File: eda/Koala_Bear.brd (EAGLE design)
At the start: 31.9 x 40 mm, 23 parts

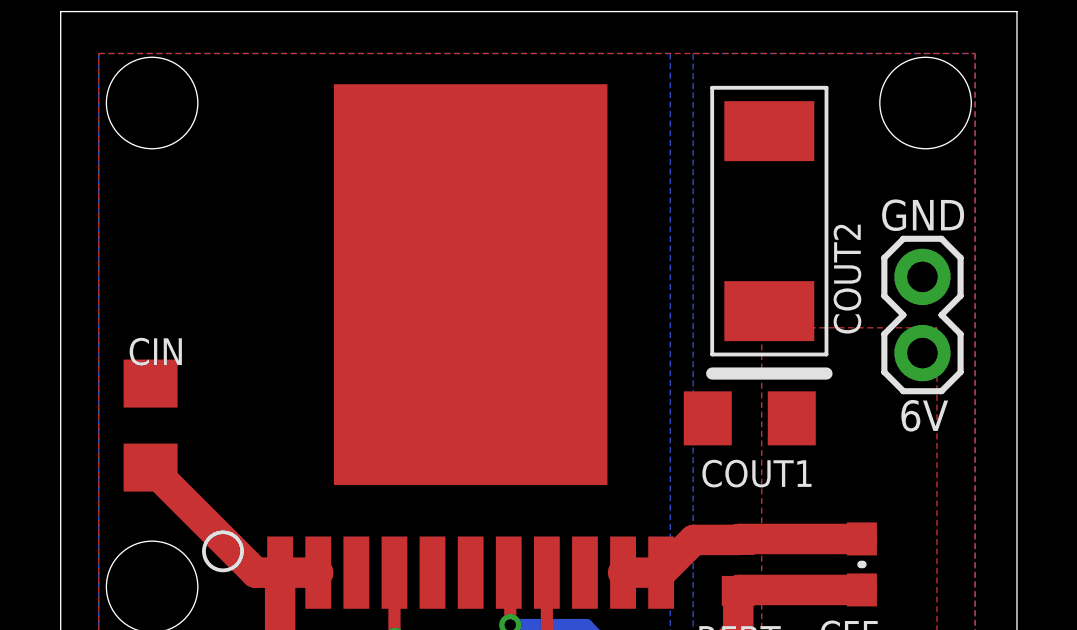
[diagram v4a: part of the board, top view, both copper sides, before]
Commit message: Ribboncable pinout fixed.
On battery_buzzer, smartsensor, and smartsensorPowered.
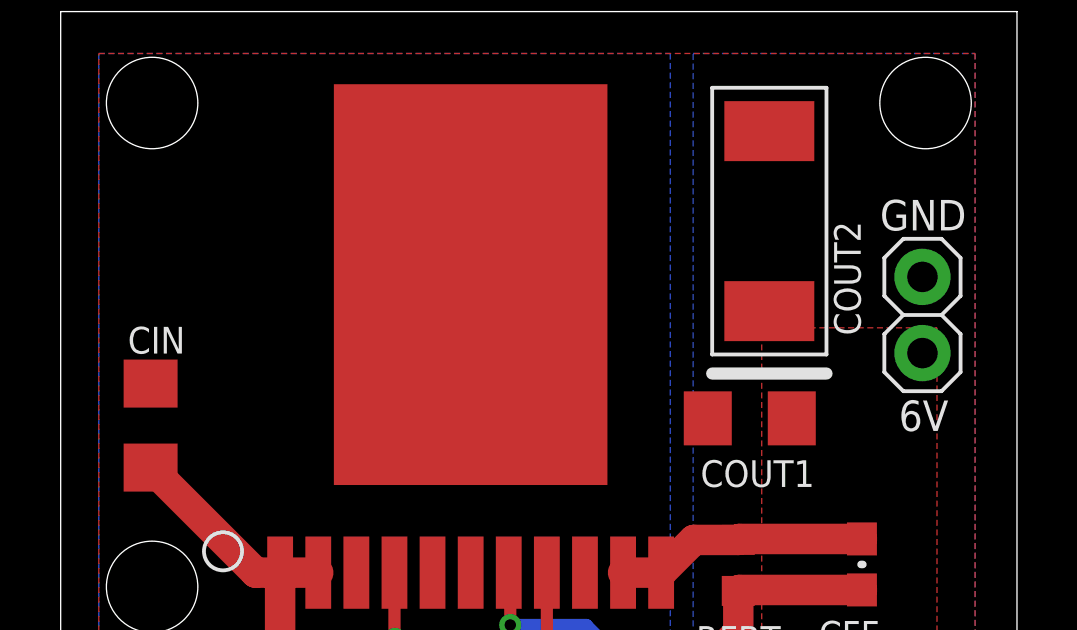
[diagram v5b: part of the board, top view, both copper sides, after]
